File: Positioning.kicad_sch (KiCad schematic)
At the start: 15 parts, among them J1 Antenna, U5 AP2127K-1.8

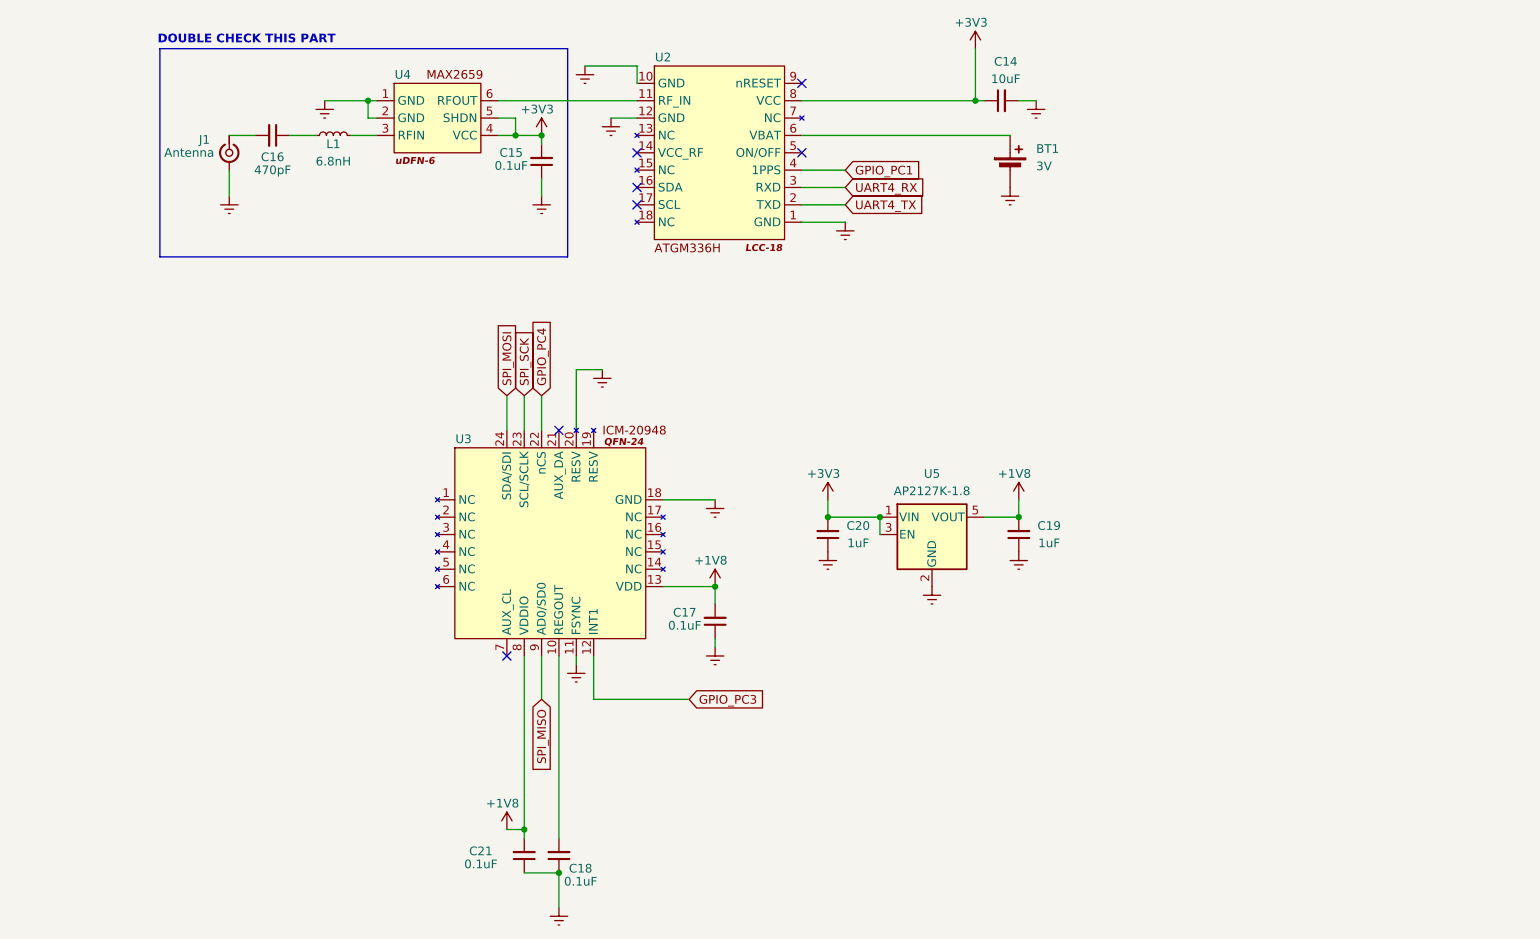
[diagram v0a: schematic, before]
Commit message: added logic shifters for IMU
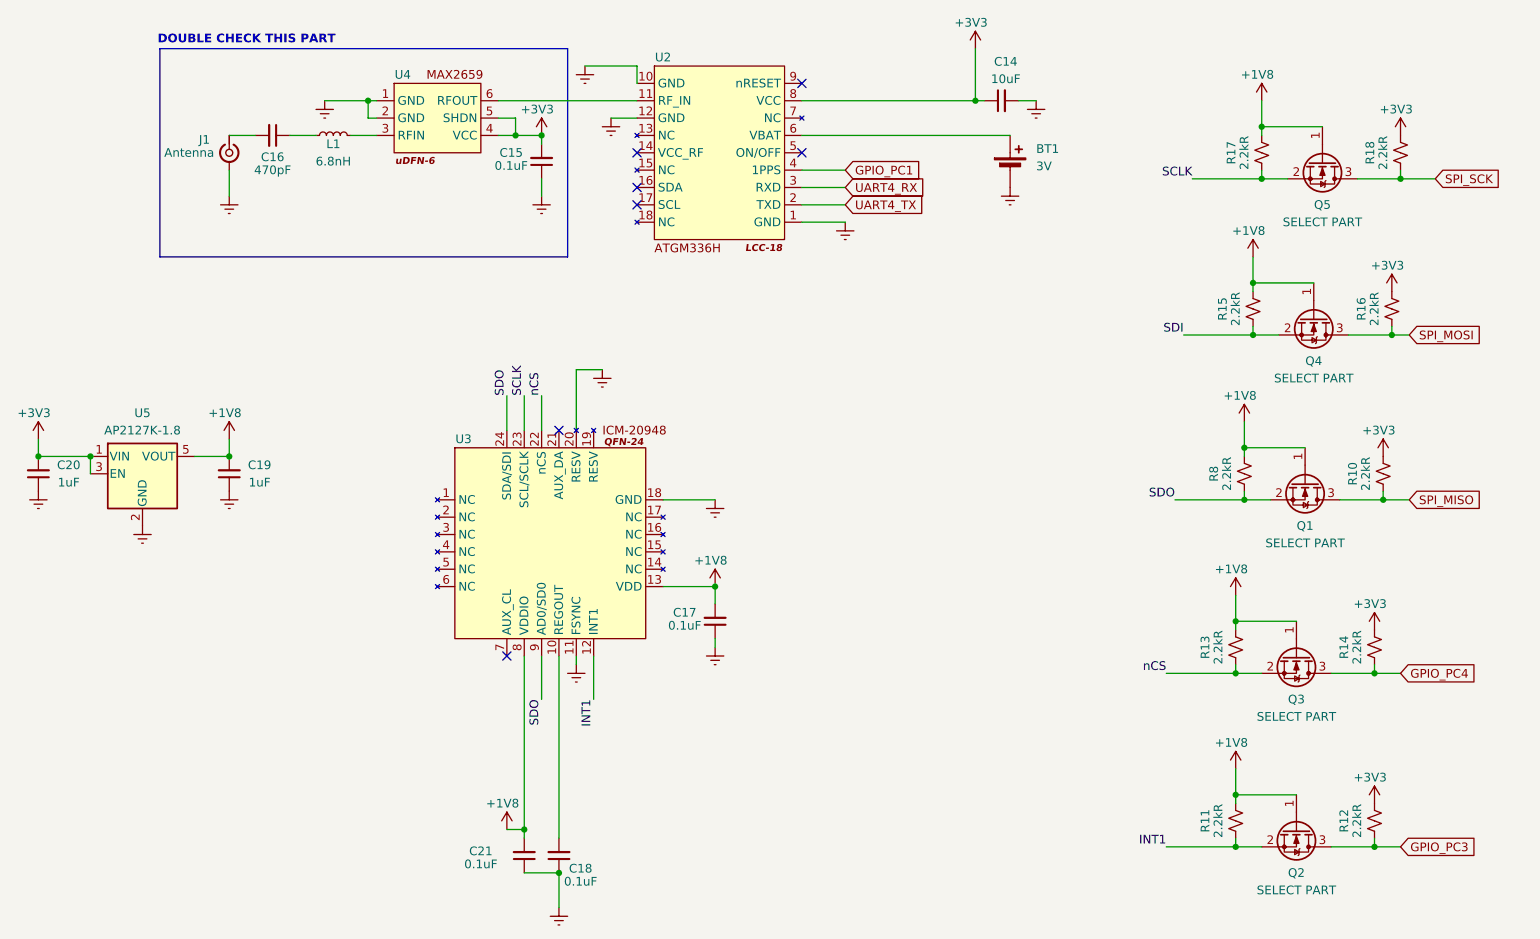
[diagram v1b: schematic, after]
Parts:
- added Q1, Q2, Q3, Q4, Q5: SELECT PART, Package_TO_SOT_SMD:SOT-23, symbol Transistor_FET:DMN2040U
- added R10, R11, R12, R13, R14, R15, R16, R17, R18, R8: 2.2kR, symbol Device:R_Small_US
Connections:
- net +1V8: now also Q1.1 (G), Q2.1 (G), Q3.1 (G), Q4.1 (G), Q5.1 (G), R11.2, R13.2, R15.2, R17.2, R8.2
- net +3V3: now also R10.2, R12.2, R14.2, R16.2, R18.2
- net GPIO_PC3: now also Q2.3 (D), R12.1; no longer U3.12 (INT1)
- net GPIO_PC4: now also Q3.3 (D), R14.1; no longer U3.22 (nCS)
- net SPI_MISO: now also Q1.3 (D), R10.1; no longer U3.9 (AD0/SD0)
- net SPI_MOSI: now also Q4.3 (D), R16.1; no longer U3.24 (SDA/SDI)
- net SPI_SCK: now also Q5.3 (D), R18.1; no longer U3.23 (SCL/SCLK)
- new net INT1: Q2.2 (S), R11.1, U3.12 (INT1)
- new net SCLK: Q5.2 (S), R17.1, U3.23 (SCL/SCLK)
- new net SDI: Q4.2 (S), R15.1
- new net SDO: Q1.2 (S), R8.1, U3.24 (SDA/SDI), U3.9 (AD0/SD0)
- new net nCS: Q3.2 (S), R13.1, U3.22 (nCS)
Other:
- moved on the sheet: C19, C20, U5

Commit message: assigned footprints
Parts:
- BT1: footprint (none) -> ML414H_IV01E:SEIKO_ML414H_IV01E
- C14, C15, C16, C17, C18, C19, C20, C21: footprint (none) -> Capacitor_SMD:C_0603_1608Metric
- J1: footprint (none) -> Connector_Coaxial:U.FL_Molex_MCRF_73412-0110_Vertical
- L1: footprint (none) -> Inductor_SMD:L_0603_1608Metric
- R10, R11, R12, R13, R14, R15, R16, R17, R18, R8: footprint (none) -> Resistor_SMD:R_0603_1608Metric
- U3: footprint (none) -> Package_DFN_QFN:QFN-24-1EP_3x3mm_P0.4mm_EP1.75x1.6mm
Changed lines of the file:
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@@
 			)
 		)
-		(property "Footprint" ""
+		(property "Footprint" "Package_DFN_QFN:QFN-24-1EP_3x3mm_P0.4mm_EP1.75x1.6mm"
 			(at 78.74 109.22 0)
 			(effects
@@
 			)
 		)
-		(property "Footprint" ""
+		(property "Footprint" "Resistor_SMD:R_0603_1608Metric"
 			(at 227.33 146.05 0)
 			(effects
@@
 			)
 		)
-		(property "Footprint" ""
+		(property "Footprint" "Resistor_SMD:R_0603_1608Metric"
 			(at 228.6 95.25 0)
 			(effects
@@
 			)
 		)
-		(property "Footprint" ""
+		(property "Footprint" "Capacitor_SMD:C_0603_1608Metric"
 			(at 193.04 40.64 0)
 			(effects
@@
 			)
 		)
-		(property "Footprint" ""
+		(property "Footprint" "Connector_Coaxial:U.FL_Molex_MCRF_73412-0110_Vertical"
 			(at 80.01 48.26 0)
 			(effects
@@
 			)
 		)
-		(property "Footprint" ""
+		(property "Footprint" "Capacitor_SMD:C_0603_1608Metric"
 			(at 86.36 45.72 0)
 			(effects
@@
 			)
 		)
-		(property "Footprint" ""
+		(property "Footprint" "Capacitor_SMD:C_0603_1608Metric"
 			(at 80.01 95.25 0)
 			(effects
@@
 			)
 		)
-		(property "Footprint" ""
+		(property "Footprint" "Resistor_SMD:R_0603_1608Metric"
 			(at 247.65 146.05 0)
 			(effects
@@
 			)
 		)
-		(property "Footprint" ""
+		(property "Footprint" "Resistor_SMD:R_0603_1608Metric"
 			(at 251.46 48.26 0)
 			(effects
@@
 			)
 		)
-		(property "Footprint" ""
+		(property "Footprint" "Inductor_SMD:L_0603_1608Metric"
 			(at 95.25 45.72 0)
 			(effects
@@
 			)
 		)
-		(property "Footprint" ""
+		(property "Footprint" "Resistor_SMD:R_0603_1608Metric"
 			(at 248.92 95.25 0)
 			(effects
@@
 			)
 		)
-		(property "Footprint" ""
+		(property "Footprint" "Capacitor_SMD:C_0603_1608Metric"
 			(at 123.19 151.13 0)
 			(effects
@@
 			)
 		)
-		(property "Footprint" ""
+		(property "Footprint" "Resistor_SMD:R_0603_1608Metric"
 			(at 247.65 120.65 0)
 			(effects
@@
 			)
 		)
-		(property "Footprint" ""
+		(property "Footprint" "Capacitor_SMD:C_0603_1608Metric"
 			(at 52.07 95.25 0)
 			(effects
@@
 			)
 		)
-		(property "Footprint" ""
+		(property "Footprint" "ML414H_IV01E:SEIKO_ML414H_IV01E"
 			(at 194.31 49.276 90)
 			(effects
@@
 			)
 		)
-		(property "Footprint" ""
+		(property "Footprint" "Resistor_SMD:R_0603_1608Metric"
 			(at 229.87 71.12 0)
 			(effects
@@
 			)
 		)
-		(property "Footprint" ""
+		(property "Footprint" "Capacitor_SMD:C_0603_1608Metric"
 			(at 125.73 49.53 0)
 			(effects
@@
 			)
 		)
-		(property "Footprint" ""
+		(property "Footprint" "Resistor_SMD:R_0603_1608Metric"
 			(at 250.19 71.12 0)
 			(effects
@@
 			)
 		)
-		(property "Footprint" ""
+		(property "Footprint" "Capacitor_SMD:C_0603_1608Metric"
 			(at 151.13 116.84 0)
 			(effects
@@
 			)
 		)
-		(property "Footprint" ""
+		(property "Footprint" "Capacitor_SMD:C_0603_1608Metric"
 			(at 128.27 151.13 0)
 			(effects
@@
 			)
 		)
-		(property "Footprint" ""
+		(property "Footprint" "Resistor_SMD:R_0603_1608Metric"
 			(at 227.33 120.65 0)
 			(effects
@@
 			)
 		)
-		(property "Footprint" ""
+		(property "Footprint" "Resistor_SMD:R_0603_1608Metric"
 			(at 231.14 48.26 0)
 			(effects

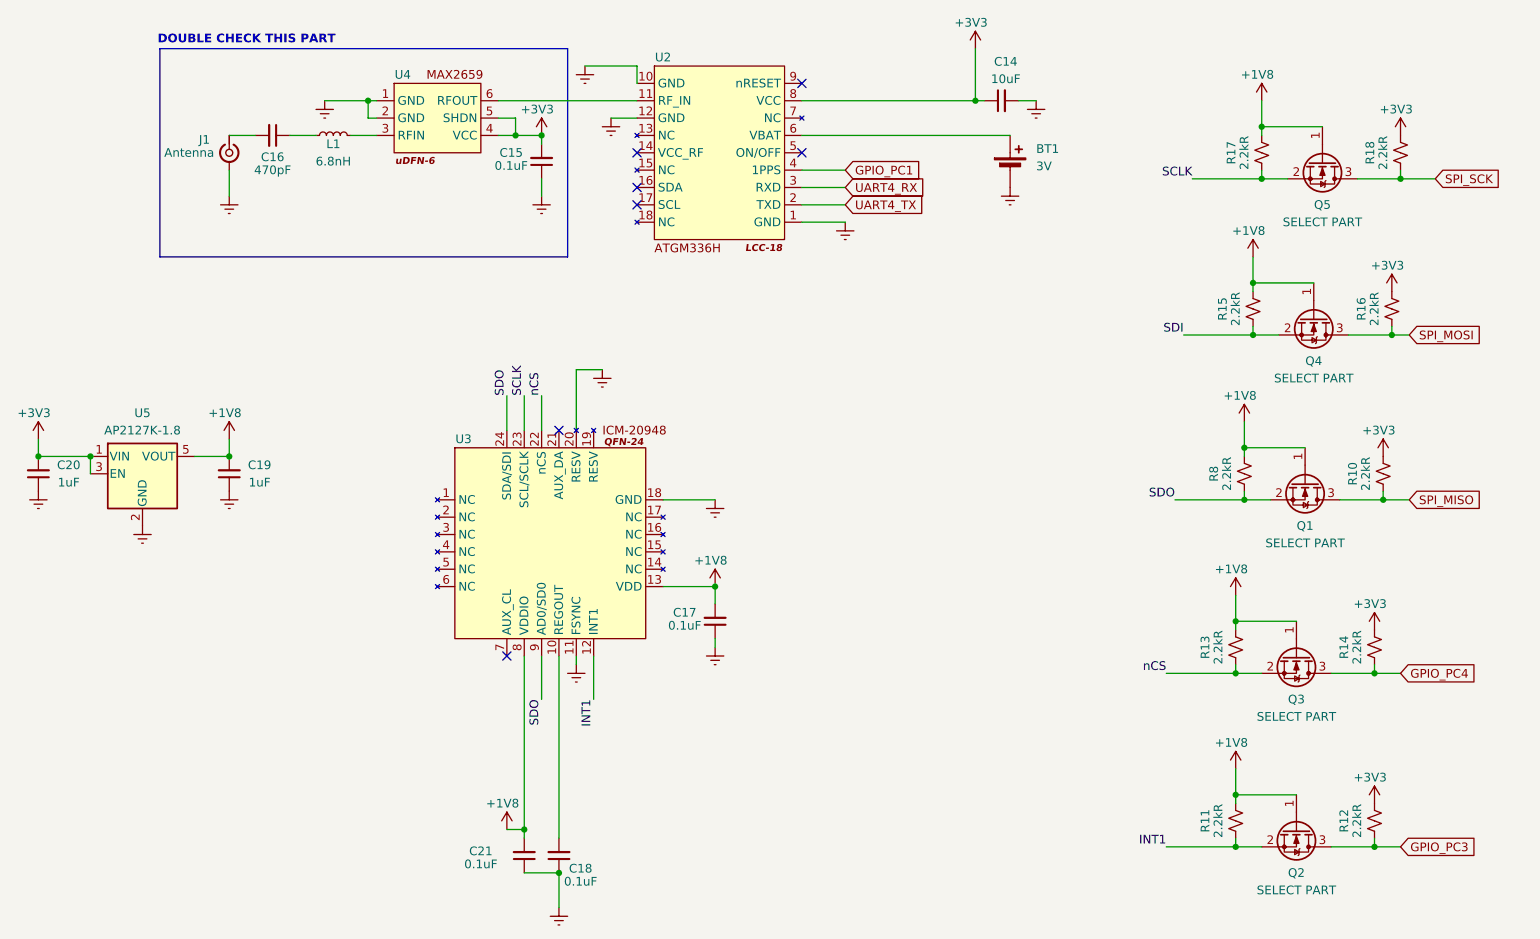
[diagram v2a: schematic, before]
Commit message: routed besides mcu connections and pwoer
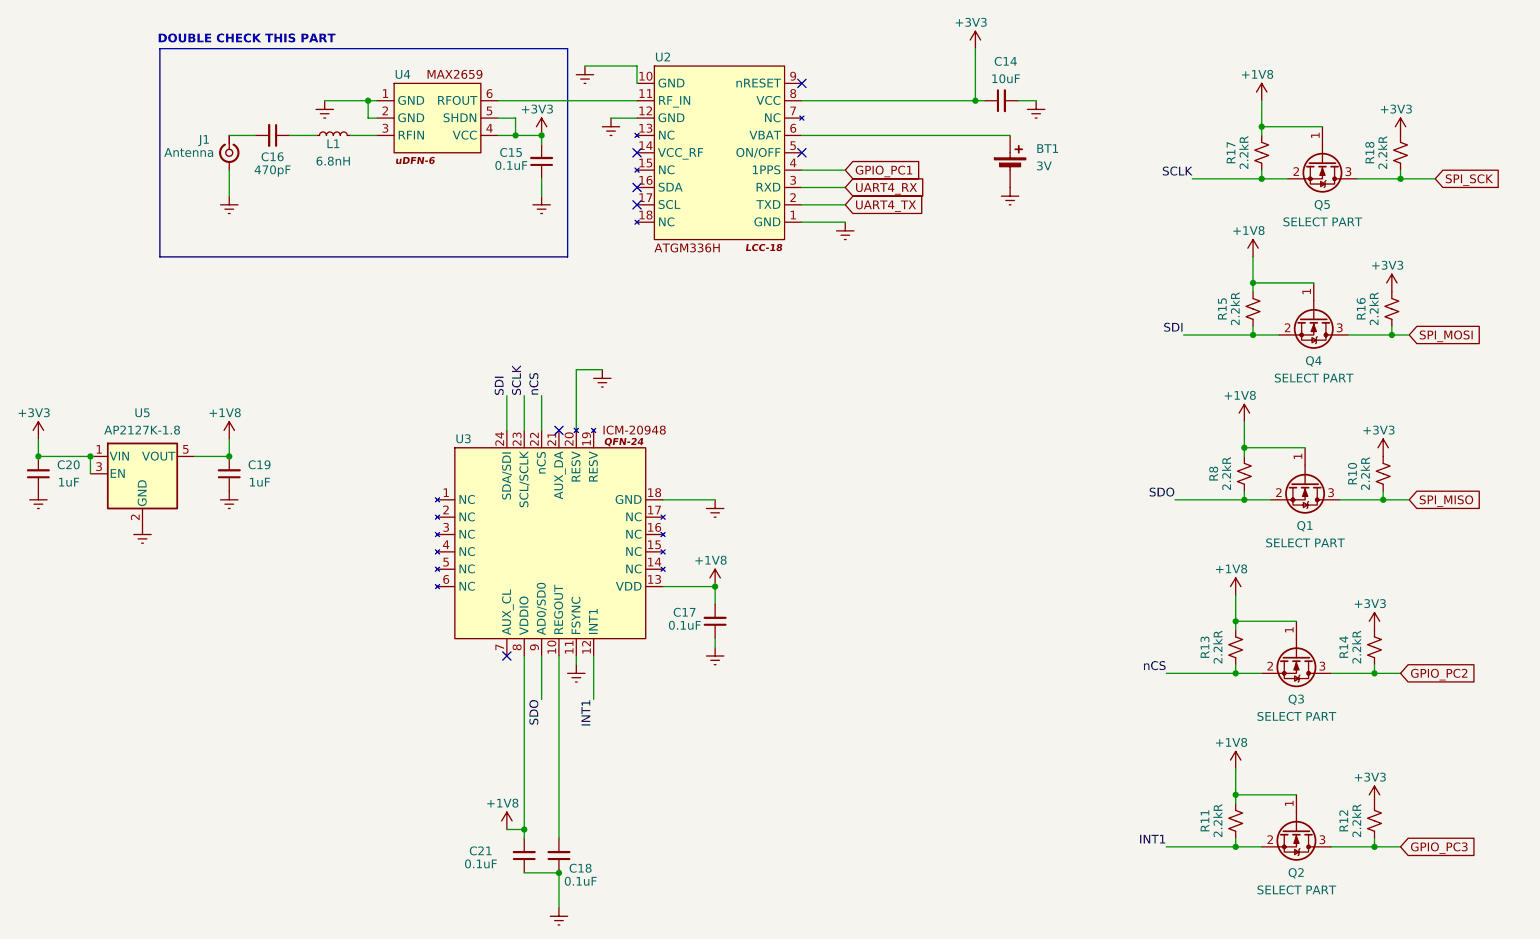
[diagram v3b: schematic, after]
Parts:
- U2: footprint (none) -> jshep:LCC-18
- U4: footprint (none) -> jshep:uDFN-6
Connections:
- net SDI: now also U3.24 (SDA/SDI)
- net SDO: no longer U3.24 (SDA/SDI)
- net GPIO_PC4 renamed GPIO_PC2
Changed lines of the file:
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@@
 		)
 	)
-	(label "SDO"
+	(label "SDI"
 		(at 120.65 83.82 90)
 		(fields_autoplaced yes)
@@
 		)
 	)
-	(global_label "GPIO_PC4"
+	(global_label "GPIO_PC2"
 		(shape input)
 		(at 251.46 124.46 0)
@@
 			)
 		)
-		(property "Footprint" ""
+		(property "Footprint" "jshep:LCC-18"
 			(at 163.83 52.07 0)
 			(effects
@@
 			)
 		)
-		(property "Footprint" ""
+		(property "Footprint" "jshep:uDFN-6"
 			(at 101.6 39.37 0)
 			(effects

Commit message: combined, submitted for Packaging Review
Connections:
- net GPIO_PC1 renamed B1
- net GPIO_PC2 renamed B2
- net GPIO_PC3 renamed B8
- net SPI_MISO renamed SPI1_MISO
- net SPI_MOSI renamed SPI1_MOSI
- net SPI_SCK renamed SPI1_SCK
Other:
- note removed: "DOUBLE CHECK THIS PART"
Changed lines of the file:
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@@
 (kicad_sch
-	(version 20231120)
+	(version 20250114)
 	(generator "eeschema")
-	(generator_version "8.0")
+	(generator_version "9.0")
 	(paper "A4")
 	(junction
@@
 		)
 	)
-	(rectangle
-		(start 69.85 33.02)
-		(end 129.54 63.5)
-		(stroke
-			(width 0)
-			(type default)
-			(color 194 0 0 1)
-		)
-		(fill
-			(type none)
-		)
-	)
-	(text "DOUBLE CHECK THIS PART"
-		(exclude_from_sim no)
-		(at 82.55 31.75 0)
-		(effects
-			(font
-				(size 1.27 1.27)
-				(thickness 0.254)
-				(bold yes)
-				(color 194 0 0 1)
-			)
-		)
-	)
 	(label "SDI"
 		(at 219.71 74.93 180)
-		(fields_autoplaced yes)
 		(effects
 			(font
@@
 	(label "SCLK"
 		(at 123.19 83.82 90)
-		(fields_autoplaced yes)
 		(effects
 			(font
@@
 	(label "SCLK"
 		(at 220.98 52.07 180)
-		(fields_autoplaced yes)
 		(effects
 			(font
@@
 	(label "INT1"
 		(at 217.17 149.86 180)
-		(fields_autoplaced yes)
 		(effects
 			(font
@@
 	(label "INT1"
 		(at 133.35 128.27 270)
-		(fields_autoplaced yes)
 		(effects
 			(font
@@
 	(label "nCS"
 		(at 217.17 124.46 180)
-		(fields_autoplaced yes)
 		(effects
 			(font
@@
 	(label "SDI"
 		(at 120.65 83.82 90)
-		(fields_autoplaced yes)
 		(effects
 			(font
@@
 	(label "SDO"
 		(at 125.73 128.27 270)
-		(fields_autoplaced yes)
 		(effects
 			(font
@@
 	(label "nCS"
 		(at 125.73 83.82 90)
-		(fields_autoplaced yes)
 		(effects
 			(font
@@
 	(label "SDO"
 		(at 218.44 99.06 180)
-		(fields_autoplaced yes)
 		(effects
 			(font
@@
 		)
 	)
-	(global_label "SPI_SCK"
+	(global_label "SPI1_SCK"
 		(shape input)
 		(at 256.54 52.07 0)
@@
 		)
 		(property "Intersheetrefs" "${INTERSHEET_REFS}"
-			(at 267.3266 52.07 0)
+			(at 268.5361 52.07 0)
 			(effects
 				(font
@@
 		)
 	)
-	(global_label "GPIO_PC1"
+	(global_label "B1"
 		(shape input)
 		(at 170.18 50.8 0)
@@
 		)
 		(property "Intersheetrefs" "${INTERSHEET_REFS}"
-			(at 182.3576 50.8 0)
+			(at 175.6447 50.8 0)
 			(effects
 				(font
@@
 		)
 	)
-	(global_label "SPI_MISO"
+	(global_label "SPI1_MISO"
 		(shape input)
 		(at 252.73 99.06 0)
@@
 		)
 		(property "Intersheetrefs" "${INTERSHEET_REFS}"
-			(at 264.3633 99.06 0)
+			(at 265.5728 99.06 0)
 			(effects
 				(font
@@
 		)
 	)
-	(global_label "SPI_MOSI"
+	(global_label "SPI1_MOSI"
 		(shape input)
 		(at 252.73 74.93 0)
@@
 		)
 		(property "Intersheetrefs" "${INTERSHEET_REFS}"
-			(at 264.3633 74.93 0)
+			(at 265.5728 74.93 0)
 			(effects
 				(font
@@
 		)
 	)
-	(global_label "GPIO_PC2"
+	(global_label "B2"
 		(shape input)
 		(at 251.46 124.46 0)
@@
 		)
 		(property "Intersheetrefs" "${INTERSHEET_REFS}"
-			(at 263.6376 124.46 0)
+			(at 256.9247 124.46 0)
 			(effects
 				(font
@@
 		)
 	)
-	(global_label "GPIO_PC3"
+	(global_label "B8"
 		(shape input)
 		(at 251.46 149.86 0)
@@
 		)
 		(property "Intersheetrefs" "${INTERSHEET_REFS}"
-			(at 263.6376 149.86 0)
+			(at 256.9247 149.86 0)
 			(effects
 				(font

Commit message: rev 1
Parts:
- Q1: renamed from Q3; value SELECT PART -> BSS138
- Q2, Q4, Q5: value SELECT PART -> BSS138
- Q3: renamed from Q1; value SELECT PART -> BSS138
- R1: renamed from R13; value 2.2kR -> 10kR
- R2: renamed from R11; value 2.2kR -> 10kR
- R3: renamed from R8; value 2.2kR -> 10kR
- R4: renamed from R15; value 2.2kR -> 10kR
- R5: renamed from R14; value 2.2kR -> 10kR
- R6: renamed from R12; value 2.2kR -> 10kR
- R7: renamed from R10; value 2.2kR -> 10kR
- R8: renamed from R16; value 2.2kR -> 10kR
- R9: renamed from R18; value 2.2kR -> 10kR
- renumbered C20 to C1, C19 to C2, C16 to C3, C21 to C4, C15 to C5, C18 to C6, C17 to C7, C14 to C8, R17 to R30, U5 to U1, U4 to U2, U2 to U4
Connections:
- net B1: no longer names the net of U4.4 (1PPS)
- net B2 renamed IMU_nCS
- net B8 renamed IMU_INT
- net UART4_RX renamed UART2_RX
- net UART4_TX renamed UART2_TX
- no-connect marks 7 -> 8
